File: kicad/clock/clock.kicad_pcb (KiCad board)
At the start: 2 copper layers, 30 parts

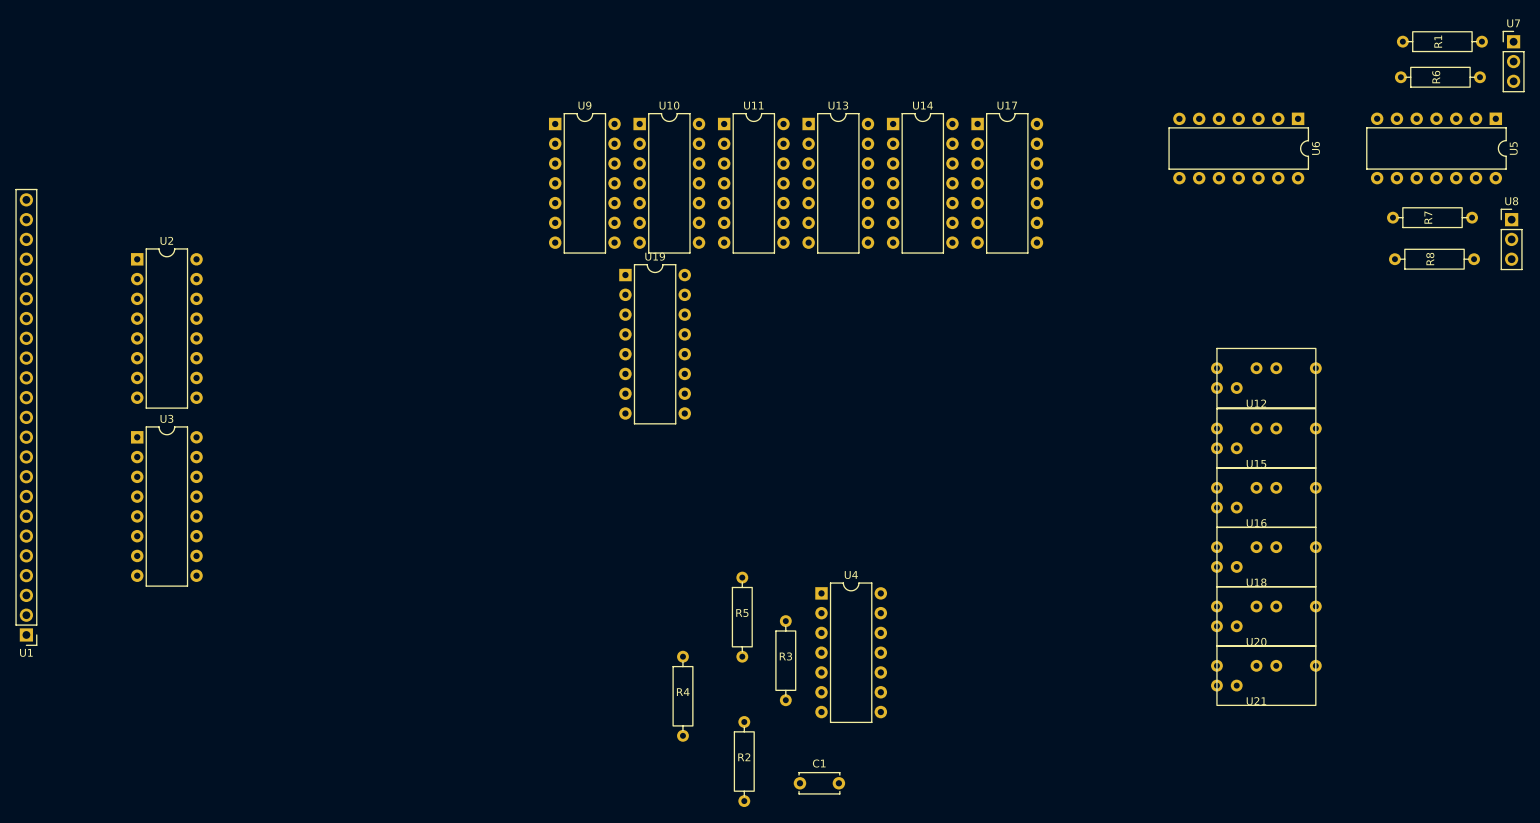
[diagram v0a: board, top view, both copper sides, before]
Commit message: Increased clock PCB clearances
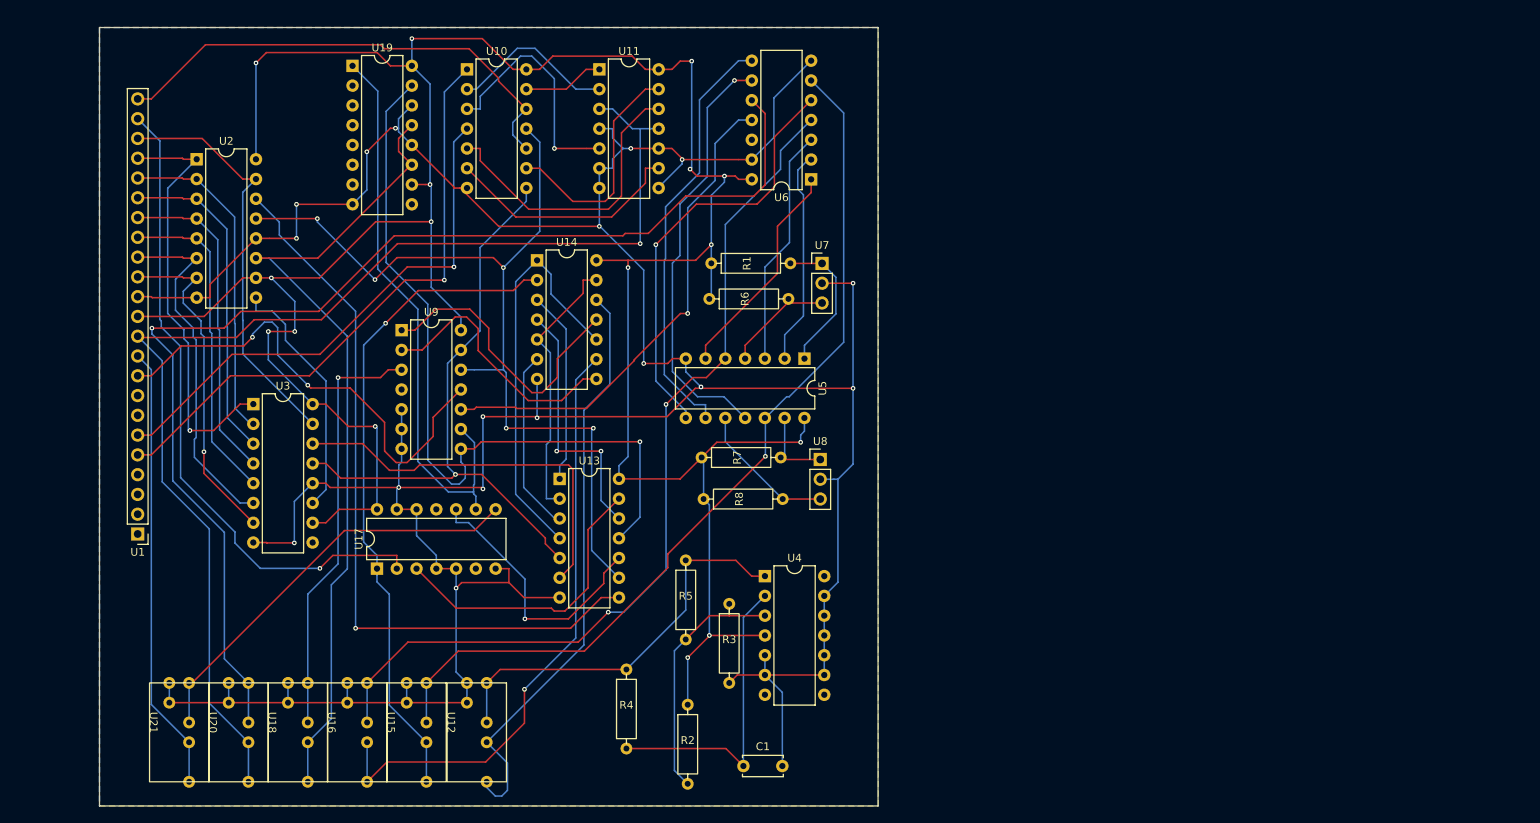
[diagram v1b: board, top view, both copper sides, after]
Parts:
- moved U21 142.2 mm to (86.4, 139.3), turned to -90 degrees
- moved U20 134.9 mm to (94.0, 139.3), turned to -90 degrees
- moved U18 128.1 mm to (101.7, 139.3), turned to -90 degrees
- moved U16 121.9 mm to (109.3, 139.3), turned to -90 degrees
- moved U15 116.4 mm to (116.9, 139.3), turned to -90 degrees
- moved U12 111.5 mm to (124.7, 139.3), turned to -90 degrees
- moved U17 96.0 mm to (115.6, 119.5), turned to 90 degrees
- moved R8 94.0 mm to (162.7, 110.6)
- moved U5 94.0 mm to (170.5, 92.5)
- moved R7 94.0 mm to (162.4, 105.2)
- moved U8 94.0 mm to (172.6, 105.5)
- moved R6 93.3 mm to (163.4, 84.9)
- moved R1 93.3 mm to (163.7, 80.3)
- moved U7 93.3 mm to (172.8, 80.3)
- moved U6 63.0 mm to (171.4, 69.5), turned to 180 degrees
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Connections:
- R7 pad 1: Net-(R7-Pad1) -> Net-(U1-V+)
- R8 pad 1: Net-(R7-Pad1) -> Net-(U1-V+)
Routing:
- net Net-(U1-GND): track 0.00 -> 469.4 mm, vias 0 -> 17
- net Net-(U1-V+): track 0.00 -> 362.6 mm, vias 0 -> 16
- net Net-(U1-CLK_B): track 0.00 -> 156.2 mm, vias 0 -> 1
- net Net-(U20-IN): track 0.00 -> 153.7 mm, vias 0 -> 1
- net Net-(U15-IN): track 0.00 -> 116.1 mm, vias 0 -> 1
- net Net-(U16-IN): track 0.00 -> 116.0 mm, vias 0 -> 2
- net Net-(U10-3Q): track 0.00 -> 115.7 mm, vias 0 -> 5
- net Net-(U18-OUT): track 0.00 -> 106.7 mm
- net Net-(U13-I4): track 0.00 -> 99.0 mm, vias 0 -> 1
- net Net-(U13-03): track 0.00 -> 95.9 mm, vias 0 -> 1
- net Net-(U14-1B): track 0.00 -> 85.2 mm, vias 0 -> 1
- net Net-(U1-FAULT): track 0.00 -> 84.2 mm, vias 0 -> 1
- net Net-(U14-4B): track 0.00 -> 79.0 mm, vias 0 -> 1
- net Net-(U10-4Q): track 0.00 -> 79.0 mm, vias 0 -> 1
- net Net-(U1-WRITE_0): track 0.00 -> 77.0 mm, vias 0 -> 1
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- added copper zone on B.Cu, net Net-(U1-GND)
- added copper zone on F.Cu, net Net-(U1-V+)
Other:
- board outline added: 100 x 100 mm

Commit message: Added pulldown resistors to clock module inputs
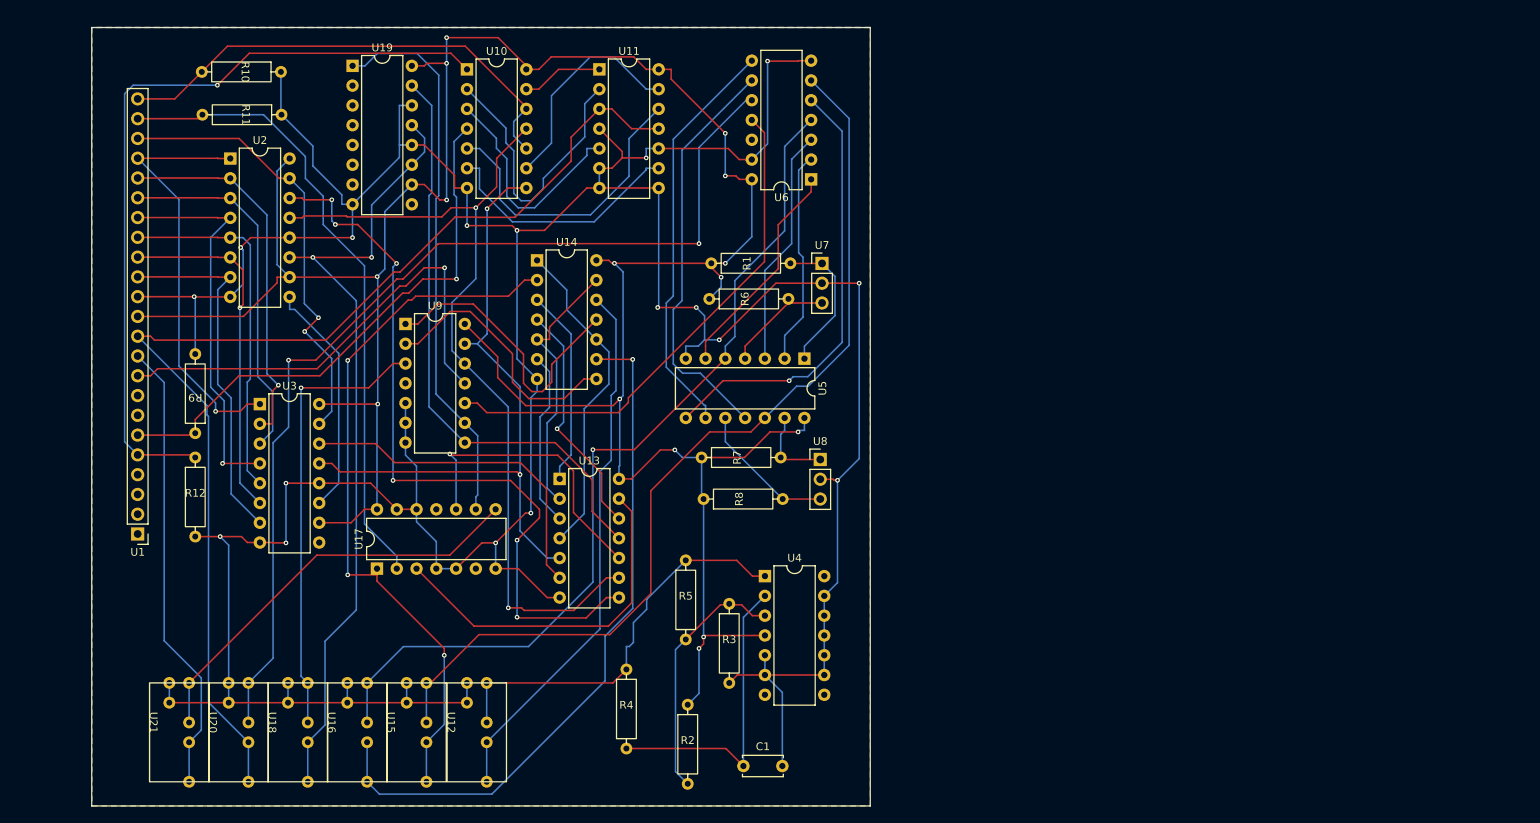
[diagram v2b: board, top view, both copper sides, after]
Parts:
- added R10: 1k, custom_footprint_library:0.4_pitch_resistor, F.Cu at (98.2, 55.7)
- added R11: 1k, custom_footprint_library:0.4_pitch_resistor, F.Cu at (98.3, 61.2)
- added R12: 1k, custom_footprint_library:0.4_pitch_resistor, F.Cu at (92.3, 110.3)
- added R9: 1k, custom_footprint_library:0.4_pitch_resistor, F.Cu at (92.3, 97.0)
- moved U2 4.32 mm to (96.8, 66.8)
- moved U9 0.94 mm to (119.3, 88.1)
- moved U3 0.85 mm to (100.6, 98.4)
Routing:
- net Net-(U1-GND): track 469.4 -> 510.2 mm
- net Net-(U1-WRITE_0): track 77.0 -> 101.6 mm
- net Net-(U20-IN): track 153.7 -> 129.2 mm, vias 1 -> 2
- net Net-(U13-I4): track 99.0 -> 76.2 mm, vias 1 -> 0
- net Net-(U10-1B): track 21.3 -> 36.5 mm
- net Net-(U1-V+): track 362.6 -> 351.0 mm, vias 16 -> 15
- net Net-(U14-4B): track 79.0 -> 89.8 mm
- net Net-(U1-CLK_B): track 156.2 -> 145.4 mm, vias 1 -> 0
- net Net-(U13-O1): track 52.5 -> 42.1 mm
- net Net-(U1-D3): track 42.1 -> 50.1 mm, vias 0 -> 1
- net Net-(U13-I5): track 38.6 -> 46.0 mm
- net Net-(U14-1B): track 85.2 -> 91.8 mm, vias 1 -> 3
- net Net-(U10-3Q): track 115.7 -> 109.1 mm, vias 5 -> 2
- net Net-(U13-O2): track 50.0 -> 43.7 mm
- net Net-(U10-4Q): track 79.0 -> 84.8 mm, vias 1 -> 2
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
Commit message: Finished IO controller schematic
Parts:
- C1: footprint Capacitor_THT:C_Disc_D5.0mm_W2.5mm_P5.00mm -> Capacitor_THT:CP_Radial_Tantal_D5.0mm_P5.00mm
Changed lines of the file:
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@@
 			(outputformat 1)
 			(mirror no)
-			(drillshape 1)
+			(drillshape 0)
 			(scaleselection 1)
-			(outputdirectory "")
+			(outputdirectory "/Users/hward/Documents/stack_machine/kicad/rendering_output/clock_order/")
 		)
 	)
@@
 		)
 	)
-	(footprint "Capacitor_THT:C_Disc_D5.0mm_W2.5mm_P5.00mm"
+	(footprint "Capacitor_THT:CP_Radial_Tantal_D5.0mm_P5.00mm"
 		(layer "F.Cu")
 		(at 162.701 144.849)
-		(descr "C, Disc series, Radial, pin pitch=5.00mm, , diameter*width=5*2.5mm^2, Capacitor, http://cdn-reichelt.de/documents/datenblatt/B300/DS_KERKO_TC.pdf")
-		(tags "C Disc series Radial pin pitch 5.00mm  diameter 5mm width 2.5mm Capacitor")
+		(descr "CP, Radial_Tantal series, Radial, pin pitch=5.00mm, , diameter=5.0mm, Tantal Electrolytic Capacitor, http://cdn-reichelt.de/documents/datenblatt/B300/TANTAL-TB-Serie%23.pdf")
+		(tags "CP Radial_Tantal series Radial pin pitch 5.00mm  diameter 5.0mm Tantal Electrolytic Capacitor")
 		(property "Reference" "C1"
-			(at 2.5 -2.5 0)
+			(at 2.5 -3.75 0)
 			(layer "F.SilkS")
 			(effects
@@
 		)
 		(property "Value" "C"
-			(at 2.5 2.5 0)
+			(at 2.5 3.75 0)
 			(layer "F.Fab")
 			(effects
@@
 			)
 		)
-		(property "Footprint" "Capacitor_THT:C_Disc_D5.0mm_W2.5mm_P5.00mm"
+		(property "Footprint" "Capacitor_THT:CP_Radial_Tantal_D5.0mm_P5.00mm"
 			(at 0 0 0)
 			(unlocked yes)
@@
 		(attr through_hole)
 		(fp_line
-			(start -0.12 -1.37)
-			(end -0.12 -1.055)
+			(start -0.304775 -1.475)
+			(end 0.195225 -1.475)
 			(stroke
 				(width 0.12)
@@
 		)
 		(fp_line
-			(start -0.12 -1.37)
-			(end 5.12 -1.37)
+			(start -0.054775 -1.725)
+			(end -0.054775 -1.225)
 			(stroke
 				(width 0.12)
@@
 			(layer "F.SilkS")
 		)
-		(fp_line
-			(start -0.12 1.055)
-			(end -0.12 1.37)
-			(stroke
-				(width 0.12)
-				(type solid)
-			)
-			(layer "F.SilkS")
-		)
-		(fp_line
-			(start -0.12 1.37)
-			(end 5.12 1.37)
-			(stroke
-				(width 0.12)
-				(type solid)
-			)
-			(layer "F.SilkS")
-		)
-		(fp_line
-			(start 5.12 -1.37)
-			(end 5.12 -1.055)
+		(fp_arc
+			(start 0.104003 -1.06)
+			(mid 2.5 -2.62)
+			(end 4.895997 -1.06)
 			(stroke
 				(width 0.12)
@@
 			(layer "F.SilkS")
 		)
-		(fp_line
-			(start 5.12 1.055)
-			(end 5.12 1.37)
+		(fp_arc
+			(start 4.895997 1.06)
+			(mid 2.5 2.62)
+			(end 0.104003 1.06)
 			(stroke
 				(width 0.12)
@@
 			(layer "F.SilkS")
 		)
-		(fp_line
-			(start -1.05 -1.5)
-			(end -1.05 1.5)
-			(stroke
-				(width 0.05)
-				(type solid)
-			)
-			(layer "F.CrtYd")
-		)
-		(fp_line
-			(start -1.05 1.5)
-			(end 6.05 1.5)
-			(stroke
-				(width 0.05)
-				(type solid)
-			)
-			(layer "F.CrtYd")
-		)
-		(fp_line
-			(start 6.05 -1.5)
-			(end -1.05 -1.5)
-			(stroke
-				(width 0.05)
-				(type solid)
-			)
-			(layer "F.CrtYd")
-		)
-		(fp_line
-			(start 6.05 1.5)
-			(end 6.05 -1.5)
+		(fp_circle
+			(center 2.5 0)
+			(end 6.22 0)
 			(stroke
 				(width 0.05)
 				(type solid)
 			)
+			(fill none)
 			(layer "F.CrtYd")
 		)
 		(fp_line
-			(start 0 -1.25)
-			(end 0 1.25)
+			(start 0.366395 -1.0875)
+			(end 0.866395 -1.0875)
 			(stroke
 				(width 0.1)
@@
 		)
 		(fp_line
-			(start 0 1.25)
-			(end 5 1.25)
+			(start 0.616395 -1.3375)
+			(end 0.616395 -0.8375)
 			(stroke
 				(width 0.1)
@@
 			(layer "F.Fab")
 		)
-		(fp_line
-			(start 5 -1.25)
-			(end 0 -1.25)
-			(stroke
-				(width 0.1)
-				(type solid)
-			)
-			(layer "F.Fab")
-		)
-		(fp_line
-			(start 5 1.25)
-			(end 5 -1.25)
+		(fp_circle
+			(center 2.5 0)
+			(end 5 0)
 			(stroke
 				(width 0.1)
 				(type solid)
 			)
+			(fill none)
 			(layer "F.Fab")
 		)
@@
 			)
 		)
-		(pad "1" thru_hole circle
+		(pad "1" thru_hole rect
 			(at 0 0)
 			(size 1.6 1.6)
@@
 			(pintype "passive")
 		)
-		(model "${KICAD8_3DMODEL_DIR}/Capacitor_THT.3dshapes/C_Disc_D5.0mm_W2.5mm_P5.00mm.wrl"
+		(model "${KICAD8_3DMODEL_DIR}/Capacitor_THT.3dshapes/CP_Radial_Tantal_D5.0mm_P5.00mm.wrl"
 			(offset
 				(xyz 0 0 0)
